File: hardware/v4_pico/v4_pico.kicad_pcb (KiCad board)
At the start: 2 copper layers, 91.3 x 95.1 mm, 95 parts, among them J1 joystick V G, J2 - LED LED strip, J3 (G) SSD1306 SPI, J4 MIDI OUT Y:M5 - R:M4, J5 Batt, J6 Neck - Y:O BK:B R:3.3, J7 Conn_01x03_Female, J8 MXP5010, Q1 2N7000, U1 74HC165, U2 74HC165, U3 74HC165, U4 Teensy3.2_breadboard_friendly

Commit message: Started PCB
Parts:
- removed J2 - LED: LED strip, Connector_JST:JST_PH_B3B-PH-K_1x03_P2.00mm_Vertical
- removed TP26: A6, TestPoint:TestPoint_THTPad_2.5x2.5mm_Drill1.2mm
- removed TP28: A1, TestPoint:TestPoint_THTPad_2.5x2.5mm_Drill1.2mm
- added C7: 100u, Capacitor_THT:CP_Radial_D7.5mm_P2.50mm, F.Cu at (228.0, 72.6)
- added C8: 100n, Capacitor_THT:C_Axial_L3.8mm_D2.6mm_P7.50mm_Horizontal, F.Cu at (195.8, -5.76)
- added D1: 1N914, Diode_THT:D_DO-34_SOD68_P7.62mm_Horizontal, F.Cu at (195.8, -9.41)
- added J10: ON/OFF, Connector_JST:JST_XH_B2B-XH-A_1x02_P2.50mm_Vertical, F.Cu at (271.4, 71.4)
- added J11: MIDI IN bk: 5 R: 4, Connector_JST:JST_XH_S2B-XH-A_1x02_P2.50mm_Horizontal, F.Cu at (178.2, 84.6)
- added J2: LED strip, Connector_JST:JST_PH_S3B-PH-K_1x03_P2.00mm_Horizontal, F.Cu at (250.3, 100.8)
- added J9: Thumb, Connector_JST:JST_PH_B5B-PH-K_1x05_P2.00mm_Vertical, F.Cu at (110.2, 73.4)
- added R32: 220, Resistor_THT:R_Axial_DIN0207_L6.3mm_D2.5mm_P7.62mm_Horizontal, F.Cu at (182.8, -2.41)
- added R33: 220, Resistor_THT:R_Axial_DIN0207_L6.3mm_D2.5mm_P7.62mm_Horizontal, F.Cu at (185.0, -8.96)
- added SW1: SW_DIP_x01, Multi_switch:Multi_switch, F.Cu at (114.6, 64.4)
- added U5: FJ08K, FJ08K:FJ08K, F.Cu at (114.7, 47.0)
- added U6: 6N138, Package_DIP:DIP-8_W7.62mm_Socket, F.Cu at (213.5, 79.8)
- added U7: MCP3002, Package_DIP:DIP-8_W7.62mm, F.Cu at (213.5, 90.9)
- C1: value 1000u -> 1000u Ch
- C3: value 100n -> 0.1 ceram
- J1: value joystick V G -> joystick
- J3: value (G) SSD1306 SPI -> SSD1306 SPI
- J4, J6: footprint Connector_JST:JST_PH_B3B-PH-K_1x03_P2.00mm_Vertical -> Connector_JST:JST_PH_S3B-PH-K_1x03_P2.00mm_Horizontal
- J5: footprint Connector_JST:JST_XH_B2B-XH-A_1x02_P2.50mm_Vertical -> Connector_JST:JST_XH_S2B-XH-A_1x02_P2.50mm_Horizontal
- J7: value Conn_01x03_Female -> 01x03
- Q1: footprint Package_TO_SOT_THT:TO-92_HandSolder -> Package_TO_SOT_THT:TO-92_Inline
- R1, R10, R11, R12, R13, R14, R15, R16, R17, R18, R19, R2, R20, R21, R22, R23, R24, R3, R4, R5, R6, R7, R8, R9: footprint Resistor_THT:R_Axial_DIN0207_L6.3mm_D2.5mm_P7.62mm_Horizontal -> Resistor_SMD:R_1206_3216Metric_Pad1.30x1.75mm_HandSolder
- TP25: value A8 -> A_in
- U1, U2, U3: footprint Package_DIP:DIP-16_W7.62mm_Socket -> Package_SO:SOIC-16_3.9x9.9mm_P1.27mm
- U4: value Teensy3.2_breadboard_friendly -> Pico; footprint teensy:Teensy30_31_32_breadboard_friendly_hand_soldering -> Raspberry Pico:RPi_Pico_SMD_TH
- moved TP14 101.1 mm to (310.3, 62.7)
- moved TP2 101.1 mm to (305.8, 63.4)
- moved TP7 101.1 mm to (305.8, 69.5)
- moved TP9 82.1 mm to (306.6, 89.0)
- moved TP11 82.1 mm to (306.7, 104.6)
- moved TP17 82.1 mm to (306.8, 76.9)
- moved TP19 82.1 mm to (306.7, 93.2)
- moved TP21 82.1 mm to (306.8, 84.8)
- moved TP23 82.1 mm to (306.7, 100.8)
- moved TP3 82.1 mm to (306.8, 80.9)
- moved TP5 82.1 mm to (306.7, 97.0)
- moved J4 58.0 mm to (207.7, 92.7)
- moved TP12 55.0 mm to (294.6, 91.2)
- moved TP24 55.0 mm to (294.4, 95.4)
- moved TP10 55.0 mm to (294.7, 74.2)
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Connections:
- C2 pad 1: +3V3 -> +3.3V
- C3 pad 1: +3V3 -> +3.3V
- C5 pad 1: +3V3 -> ADC_VREF
- J1 pad 1: GND -> GNDA
- J1 pad 2: +3V3 -> ADC_VREF
- J3 pad 2: +3V3 -> +3.3V
- J3 pad 3: Net-(J3-Pad3) -> ADC_CLK
- J3 pad 4: Net-(J3-Pad4) -> ADC_DIN
- J5 pad 1: GND -> Net-(J10-Pad1)
- J6 pad 3: +3V3 -> ADC_VREF
- Q1 pad 2: +3V3 -> +3.3V
- R1 pad 2: +3V3 -> +3.3V
- R10 pad 2: +3V3 -> +3.3V
- R11 pad 2: +3V3 -> +3.3V
- R12 pad 2: +3V3 -> +3.3V
- R13 pad 2: +3V3 -> +3.3V
- R14 pad 2: +3V3 -> +3.3V
- R15 pad 2: +3V3 -> +3.3V
- R16 pad 2: +3V3 -> +3.3V
- R17 pad 2: +3V3 -> +3.3V
- R18 pad 2: +3V3 -> +3.3V
- R19 pad 2: +3V3 -> +3.3V
- R2 pad 2: +3V3 -> +3.3V
- R20 pad 2: +3V3 -> +3.3V
- R21 pad 2: +3V3 -> +3.3V
- R22 pad 2: +3V3 -> +3.3V
- R23 pad 2: +3V3 -> +3.3V
- R24 pad 2: +3V3 -> +3.3V
- R27 pad 1: +3V3 -> +3.3V
- R3 pad 2: +3V3 -> +3.3V
- R30 pad 1: +3V3 -> +3.3V
- R4 pad 2: +3V3 -> +3.3V
- R5 pad 2: +3V3 -> +3.3V
- R6 pad 2: +3V3 -> +3.3V
- R7 pad 2: +3V3 -> +3.3V
- R8 pad 2: +3V3 -> +3.3V
- R9 pad 2: +3V3 -> +3.3V
- TP13 pad 1: +3V3 -> +3.3V
- TP27 pad 1: +3V3 -> +3.3V
- TP29 pad 1: +3V3 -> +3.3V
- U1 pad 15: /SR_CLK_INH -> GND
- U1 pad 16: +3V3 -> +3.3V
- U2 pad 15: /SR_CLK_INH -> GND
- U2 pad 16: +3V3 -> +3.3V
- U3 pad 15: /SR_CLK_INH -> GND
- U3 pad 16: +3V3 -> +3.3V
- U4 pad 1: GND -> Net-(R26-Pad2)
- U4 pad 10: /SR_DO -> Net-(J3-Pad5)
- U4 pad 11: /SR_CLK_INH -> unconnected-(U4-Pad11)
- U4 pad 12: unconnected-(U4-Pad12) -> ADC_CS
- U4 pad 13: Net-(J3-Pad4) -> unconnected-(U4-Pad13)
- U4 pad 14: Net-(J3-Pad5) -> /SR_CLK
- U4 pad 2: unconnected-(U4-Pad2) -> Net-(R32-Pad1)
- U4 pad 20: Net-(J3-Pad3) -> unconnected-(U4-Pad20)
- U4 pad 21: /SR_CLK -> unconnected-(U4-Pad21)
- U4 pad 22: Net-(TP28-Pad1) -> unconnected-(U4-Pad22)
- U4 pad 23: Net-(J1-Pad5) -> unconnected-(U4-Pad23)
- U4 pad 24: Net-(J1-Pad4) -> unconnected-(U4-Pad24)
- U4 pad 25: Net-(J1-Pad3) -> Net-(TP31-Pad1)
- U4 pad 26: Net-(J6-Pad2) -> Net-(TP30-Pad1)
- U4 pad 27: Net-(TP26-Pad1) -> Net-(Q1-Pad1)
- U4 pad 28: /batt_check -> unconnected-(U4-Pad28)
- U4 pad 29: Net-(TP25-Pad1) -> Net-(J1-Pad5)
- U4 pad 3: Net-(R26-Pad2) -> GND
- U4 pad 30: Net-(Q1-Pad1) -> unconnected-(U4-Pad30)
- U4 pad 31: +3V3 -> Net-(J6-Pad2)
- U4 pad 32: unconnected-(U4-Pad32) -> Net-(J1-Pad4)
- U4 pad 33: +5V -> GNDA
- U4 pad 4: Net-(TP31-Pad1) -> ADC_CLK
- U4 pad 5: Net-(TP30-Pad1) -> ADC_DIN
- U4 pad 6: Net-(J3-Pad7) -> ADC_DOUT
- U4 pad 7: unconnected-(U4-Pad7) -> Net-(J3-Pad7)
- U4 pad 8: Net-(J3-Pad6) -> unconnected-(U4-Pad8)
- U4 pad 9: /SR_SH -> Net-(J3-Pad6)
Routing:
- net +3V3: track 242.9 -> 0.00 mm
- net GND: track 207.4 -> 0.00 mm
- net +5V: track 113.4 -> 0.00 mm
- net /SR_SH: track 84.3 -> 0.00 mm
- net /SR_CLK_INH: track 81.4 -> 0.00 mm
- net /SR_CLK: track 79.1 -> 0.00 mm
- net Net-(R2-Pad1): track 77.5 -> 0.00 mm
- net Net-(R14-Pad1): track 62.9 -> 0.00 mm
- net Net-(Q1-Pad1): track 59.9 -> 0.00 mm
- net Net-(R1-Pad1): track 56.1 -> 0.00 mm
- net Net-(R3-Pad1): track 48.7 -> 0.00 mm
- net Net-(U1-Pad10): track 46.2 -> 0.00 mm
- net Net-(R15-Pad1): track 44.9 -> 0.00 mm
- net Net-(R4-Pad1): track 44.9 -> 0.00 mm
- net Net-(J6-Pad1): track 33.3 -> 0.00 mm
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- removed copper zone on B.Cu, net GND
- removed copper zone on F.Cu, net GND
- removed copper zone on B.Cu, net Net-(C4-Pad1)
- removed copper zone on F.Cu, net Net-(C4-Pad1)
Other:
- board text added: "TES sax v4 SPI SSD1306 LED strip RP2040"
- board text removed: "TES sax v3 SPI SSD1306 LED stripe"
- board text removed: "TES sax v3.2 SPI SSD1306 LED strip"

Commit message: Work on PCB
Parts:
- C7: footprint Capacitor_THT:CP_Radial_D7.5mm_P2.50mm -> Capacitor_THT:CP_Radial_D6.3mm_P2.50mm
- J3: footprint Connector_PinSocket_2.54mm:PinSocket_1x07_P2.54mm_Vertical -> Connector_JST:JST_PH_S7B-PH-K_1x07_P2.00mm_Horizontal
- moved C8 125.6 mm to (153.6, 112.5)
- moved D1 125.6 mm to (153.6, 108.9)
- moved R33 125.6 mm to (142.8, 109.3)
- moved R32 111.8 mm to (164.7, 108.0)
- moved C7 71.7 mm to (169.0, 113.4)
- moved U6 55.4 mm to (159.6, 93.0)
- moved J11 26.7 mm to (152.3, 91.2)

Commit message: Trying to place everythin on pcb...
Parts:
- J10: footprint Connector_JST:JST_XH_B2B-XH-A_1x02_P2.50mm_Vertical -> Connector_JST:JST_XH_S2B-XH-A_1x02_P2.50mm_Horizontal
- J3: footprint Connector_JST:JST_PH_S7B-PH-K_1x07_P2.00mm_Horizontal -> Connector_JST:JST_PH_B7B-PH-K_1x07_P2.00mm_Vertical
- moved R33 77.9 mm to (219.8, 97.1)
- moved C8 77.0 mm to (224.7, 83.1)
- moved J11 72.1 mm to (223.7, 101.5)
- moved C7 71.2 mm to (235.6, 88.2)
- moved R32 66.8 mm to (230.0, 93.8), turned to 90 degrees
- moved D1 66.7 mm to (216.3, 86.2), turned to -90 degrees
- moved U6 59.8 mm to (219.1, 86.2)
- moved J3 48.0 mm to (226.4, 73.9), turned to 0 degrees
- moved TP32 44.4 mm to (194.9, 79.2)
- moved TP13 38.8 mm to (194.9, 72.9)
- moved C1 33.7 mm to (242.7, 87.8)
- moved J4 31.1 mm to (206.1, 61.7), turned to 0 degrees
- moved R31 22.2 mm to (231.0, 68.1)
- moved R25 22.1 mm to (234.1, 68.1)
- moved J10 20.8 mm to (250.8, 74.4)
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
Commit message: Initial routing
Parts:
- removed TP13: 3.3, TestPoint:TestPoint_THTPad_2.5x2.5mm_Drill1.2mm
- J5, J6: moved to B.Cu
- Q1: footprint Package_TO_SOT_THT:TO-92_Inline -> Package_TO_SOT_THT:TO-92L_HandSolder
- moved TP14 103.3 mm to (214.2, 100.8)
- moved TP9 94.5 mm to (214.2, 109.0)
- moved TP17 94.1 mm to (218.3, 109.0)
- moved TP21 93.2 mm to (215.8, 104.9)
- moved TP7 86.7 mm to (223.5, 96.8)
- moved TP18 85.3 mm to (211.7, 104.9)
- moved TP5 85.2 mm to (222.4, 109.0)
- moved TP2 85.0 mm to (227.6, 96.8)
- moved TP23 80.7 mm to (226.4, 109.0)
- moved TP1 80.4 mm to (222.4, 100.8)
- moved TP22 79.7 mm to (218.3, 100.8)
- moved TP8 78.3 mm to (230.5, 100.8)
- moved TP19 77.8 mm to (230.5, 109.0)
- moved TP24 75.2 mm to (219.8, 104.9)
- moved TP16 75.1 mm to (226.4, 100.8)
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- renumbered G*** to owl_beak, G*** to owl_big_pcb, G*** to owl_small_pcb
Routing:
- net GND: track 0.00 -> 275.8 mm, vias 0 -> 3
- net +3.3V: track 0.00 -> 266.2 mm, vias 0 -> 2
- net Net-(R5-Pad1): track 0.00 -> 182.5 mm, vias 0 -> 6
- net +5V: track 0.00 -> 142.5 mm
- net Net-(R3-Pad1): track 0.00 -> 140.2 mm, vias 0 -> 3
- net Net-(R15-Pad1): track 0.00 -> 129.0 mm, vias 0 -> 3
- net Net-(J3-Pad5): track 0.00 -> 124.1 mm, vias 0 -> 4
- net Net-(R2-Pad1): track 0.00 -> 112.7 mm, vias 0 -> 5
- net /SR_SH: track 0.00 -> 106.1 mm, vias 0 -> 3
- net Net-(R7-Pad1): track 0.00 -> 100.1 mm, vias 0 -> 1
- net Net-(R14-Pad1): track 0.00 -> 94.9 mm, vias 0 -> 5
- net ADC_CS: track 0.00 -> 87.5 mm, vias 0 -> 1
- net Net-(J3-Pad6): track 0.00 -> 81.4 mm, vias 0 -> 3
- net Net-(R6-Pad1): track 0.00 -> 80.2 mm
- net Net-(R24-Pad1): track 0.00 -> 77.9 mm, vias 0 -> 1
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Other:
- board size 91.3 x 95.1 mm -> 54.2 x 95.1 mm

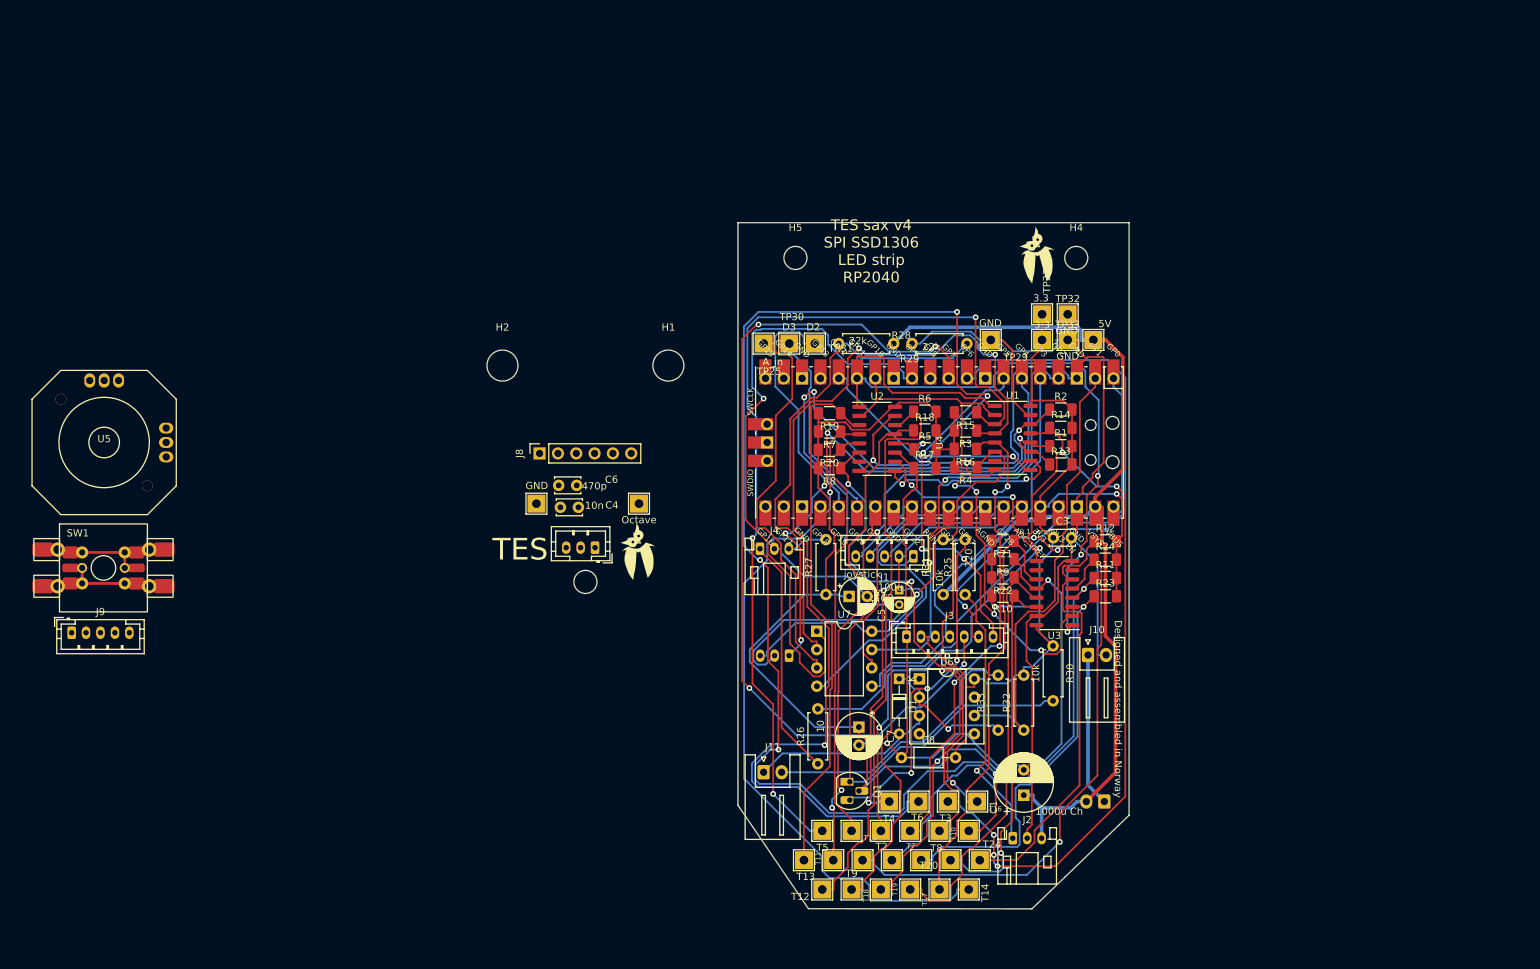
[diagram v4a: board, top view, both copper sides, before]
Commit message: Improved silk
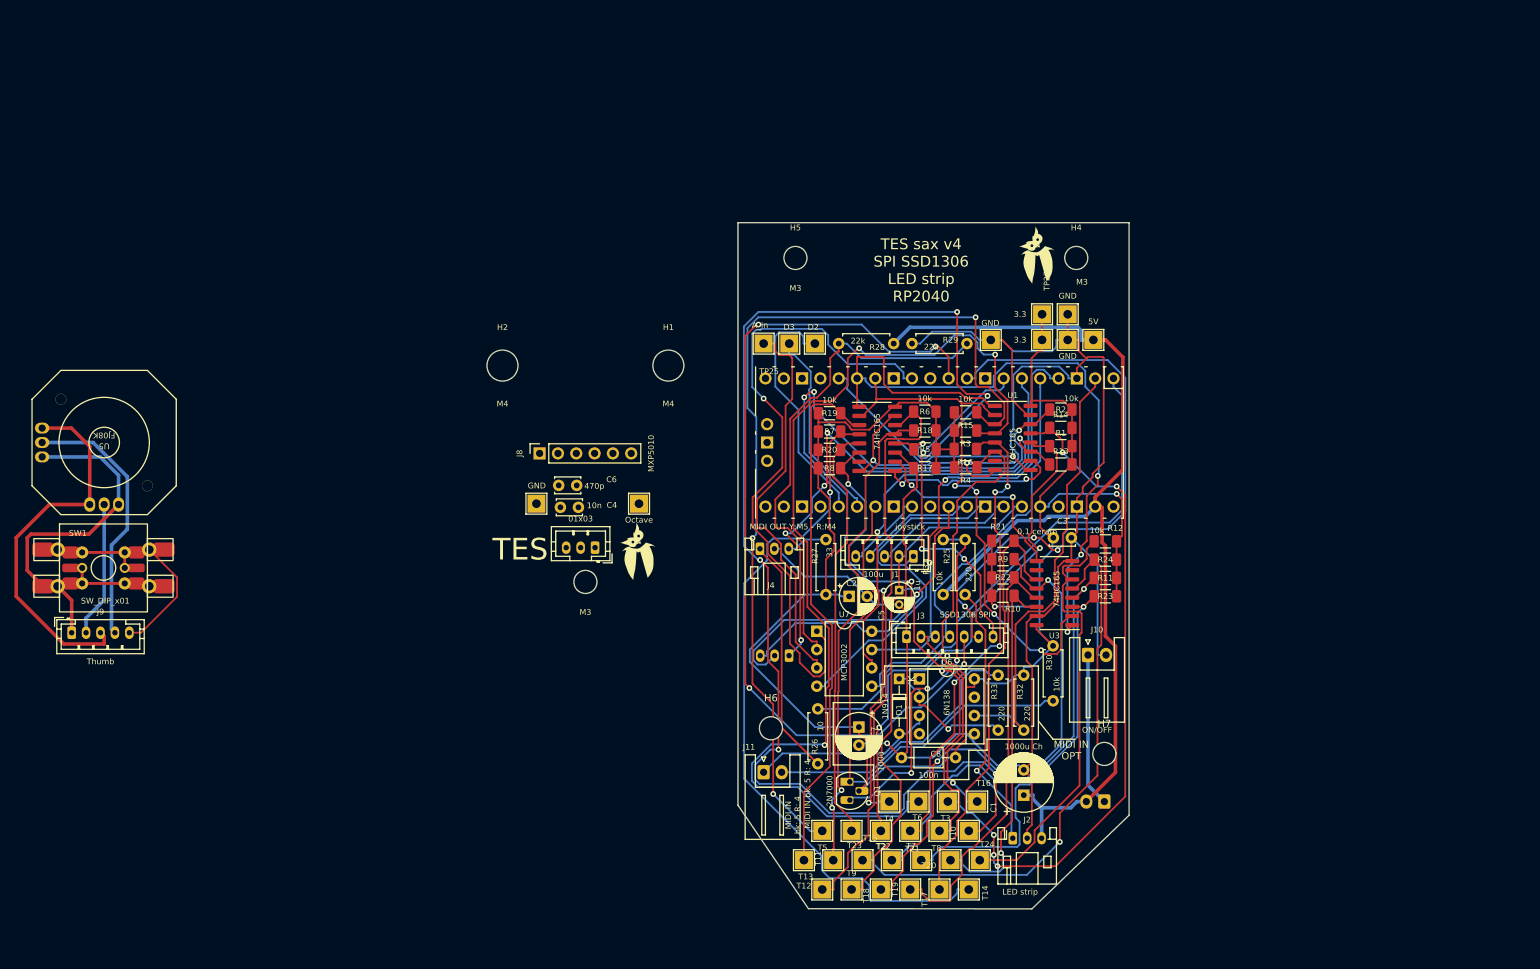
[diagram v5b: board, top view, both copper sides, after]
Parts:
- added H6: M3, MountingHole:MountingHole_3.2mm_M3, F.Cu at (207.1, 86.6)
- added H7: M3, MountingHole:MountingHole_3.2mm_M3, F.Cu at (253.4, 90.2)
- U4: footprint Raspberry Pico:RPi_Pico_SMD_TH -> Raspberry Pico:RPi_Pico_TH
- turned U5 to 180 degrees
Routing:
- net Net-(J9-Pad3): track 0.00 -> 52.7 mm
- net Net-(J9-Pad1): track 0.00 -> 45.2 mm
- net Net-(J9-Pad4): track 0.00 -> 36.5 mm
- net Net-(J9-Pad2): track 0.00 -> 18.8 mm
- net Net-(J9-Pad5): track 0.00 -> 16.8 mm
- net ADC_CS: track 87.5 -> 88.9 mm
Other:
- board text added: "MIDI IN OPT"
- board text added: "MIDI IN bk: 5 R: 4"
- board text added: "Neck Y:O BK:B R:3.3"

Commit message: Check on courtyarb, placing
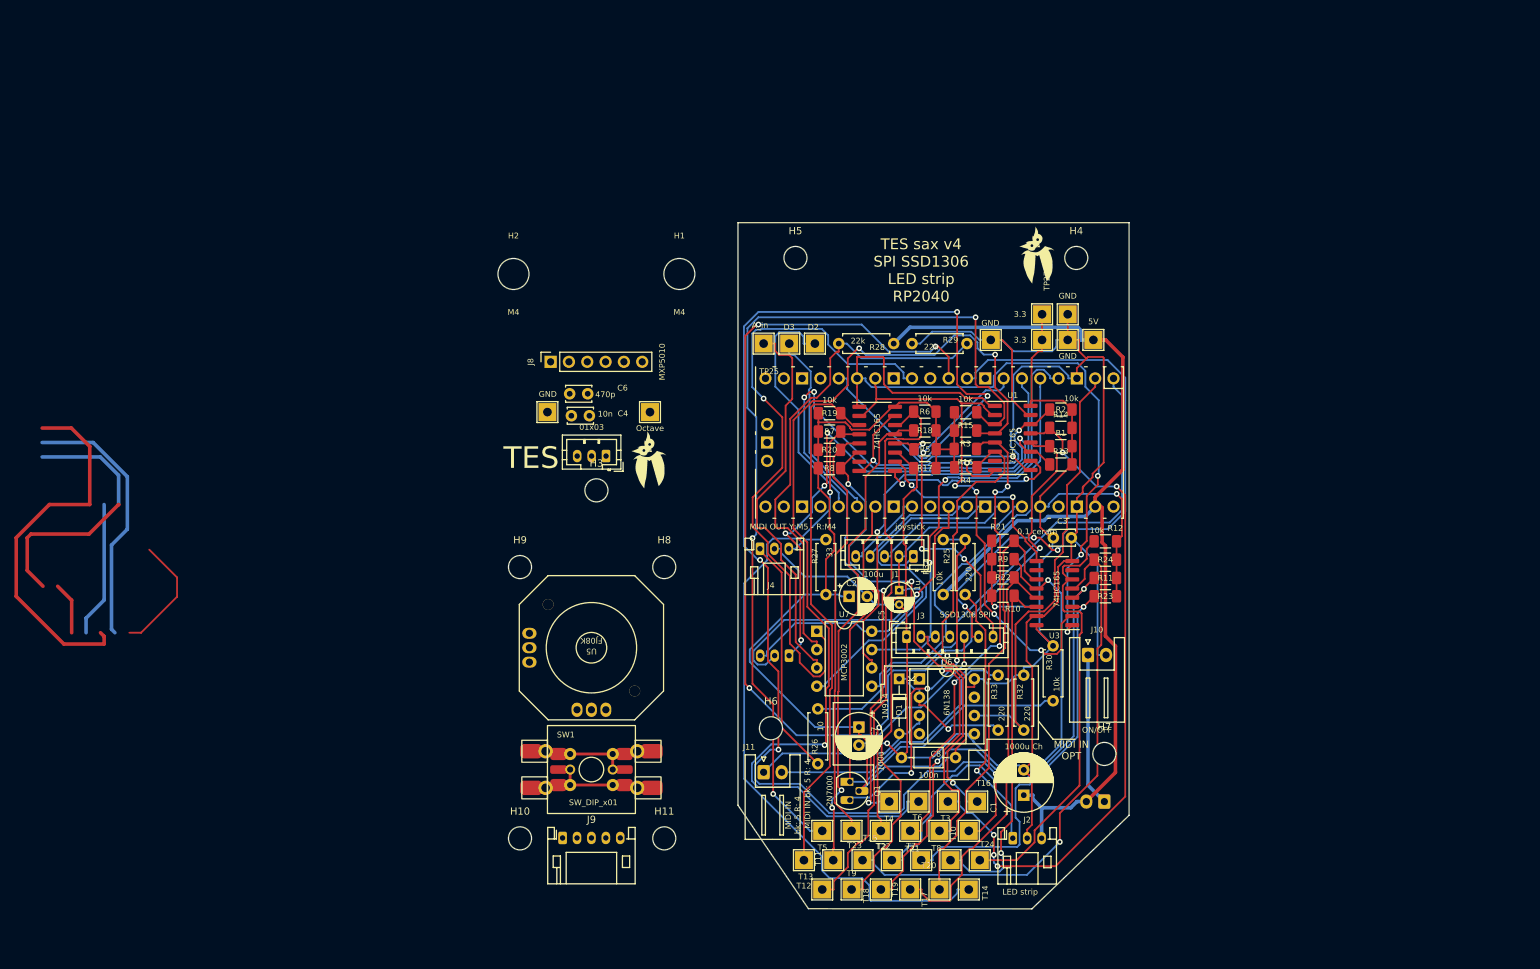
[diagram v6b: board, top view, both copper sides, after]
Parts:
- added H10: M3, MountingHole:MountingHole_3.2mm_M3_ISO14580, F.Cu at (172.3, 101.9)
- added H11: M3, MountingHole:MountingHole_3.2mm_M3_ISO14580, F.Cu at (192.3, 101.9)
- added H8: M3, MountingHole:MountingHole_3.2mm_M3_ISO14580, F.Cu at (192.3, 64.3)
- added H9: M3, MountingHole:MountingHole_3.2mm_M3_ISO14580, F.Cu at (172.3, 64.3)
- H3, H4, H5, H6, H7: footprint MountingHole:MountingHole_3.2mm_M3 -> MountingHole:MountingHole_3.2mm_M3_ISO14580
- J9: footprint Connector_JST:JST_PH_B5B-PH-K_1x05_P2.00mm_Vertical -> Connector_JST:JST_PH_S5B-PH-K_1x05_P2.00mm_Horizontal
- moved J9 73.8 mm to (178.2, 101.8)
- moved U5 73.3 mm to (182.2, 75.4)
- moved SW1 73.2 mm to (182.2, 92.3)
- moved C6 12.8 mm to (181.7, 40.2)
- moved H1 12.8 mm to (194.4, 23.6)
- moved H2 12.8 mm to (171.4, 23.6)
- moved H3 12.8 mm to (182.9, 53.6)
- moved J8 12.8 mm to (176.6, 35.8)
- moved TP36 12.8 mm to (190.4, 42.8)
- moved TP37 12.8 mm to (176.1, 42.8)
- moved owl_beak 12.8 mm to (190.2, 49.6)
- moved C4 12.8 mm to (182.0, 43.3)
- moved J7 12.8 mm to (184.3, 48.9)
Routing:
- net Net-(R15-Pad1): track 129.0 -> 344.6 mm, vias 3 -> 9
- net Net-(R5-Pad1): track 182.5 -> 0.00 mm, vias 6 -> 0
- net Net-(R24-Pad1): track 77.9 -> 0.00 mm, vias 1 -> 0
- net +5V: track 142.5 -> 220.3 mm, vias 0 -> 1
- net Net-(J4-Pad1): track 33.1 -> 0.00 mm

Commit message: Trying to make room
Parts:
- moved U4 1.00 mm to (229.5, 47.0)
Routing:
- net Net-(R15-Pad1): track 344.6 -> 0.00 mm, vias 9 -> 0
- net GND: track 275.8 -> 0.00 mm, vias 3 -> 0
- net +3.3V: track 266.2 -> 0.00 mm, vias 2 -> 0
- net +5V: track 220.3 -> 0.00 mm, vias 1 -> 0
- net Net-(R3-Pad1): track 140.2 -> 0.00 mm, vias 3 -> 0
- net Net-(J3-Pad5): track 123.7 -> 0.00 mm, vias 4 -> 0
- net Net-(R2-Pad1): track 112.7 -> 0.00 mm, vias 5 -> 0
- net /SR_SH: track 106.1 -> 0.00 mm, vias 3 -> 0
- net Net-(R7-Pad1): track 100.1 -> 0.00 mm, vias 1 -> 0
- net Net-(R14-Pad1): track 94.9 -> 0.00 mm, vias 5 -> 0
- net ADC_CS: track 88.9 -> 0.00 mm, vias 1 -> 0
- net Net-(J3-Pad6): track 81.4 -> 0.00 mm, vias 3 -> 0
- net Net-(R6-Pad1): track 80.2 -> 0.00 mm
- net Net-(J6-Pad1): track 75.2 -> 0.00 mm, vias 5 -> 0
- net Net-(R9-Pad1): track 74.9 -> 0.00 mm, vias 2 -> 0
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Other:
- board size 54.2 x 95.1 mm -> 92.3 x 96 mm
